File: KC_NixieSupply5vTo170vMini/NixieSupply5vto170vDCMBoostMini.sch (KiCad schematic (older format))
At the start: 40 parts, among them J1 Screw_Terminal_01x04, J2 CONN_01X01, J3 CONN_01X01, J4 CONN_01X01, J5 CONN_01X01, P1 USB_OTG, Q1 FDS2672CT, Q26 MMBTA42, U1 UCC3803

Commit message: Corrected the C6 BOM entry.   Also created a BOM for the MINI version of the layout.
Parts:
- C6: MPN (none) -> C0805C101JAGAC7800
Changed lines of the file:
@@
 F 1 "100pF 250v" H 6700 2200 50  0000 L CNN
 F 2 "Capacitors_SMD:C_0805" H 6738 2250 50  0001 C CNN
-F 3 "" H 6700 2400 50  0000 C CNN
+F 3 "https://www.digikey.com/products/en/capacitors/ceramic-capacitors/60?k=C0805C101JAGAC7800&k=&pkeyword=C0805C101JAGAC7800&pv7=2&quantity=0&ColumnSort=0&page=1&pageSize=25" H 6700 2400 50  0001 C CNN
+F 4 "C0805C101JAGAC7800" H 6700 2400 60  0001 C CNN "MPN"
 	1    6700 2400
 	1    0    0    -1

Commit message: test update
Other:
- moved on the sheet: R7
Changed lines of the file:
@@
 L R R7
 U 1 1 5A408EBF
-P 3050 2650
-F 0 "R7" V 3130 2650 50  0000 C CNN
-F 1 "2k" V 3050 2650 50  0000 C CNN
-F 2 "Resistors_SMD:R_0805" V 2980 2650 50  0001 C CNN
-F 3 "" H 3050 2650 50  0000 C CNN
-	1    3050 2650
+P 2950 2650
+F 0 "R7" V 3030 2650 50  0000 C CNN
+F 1 "2k" V 2950 2650 50  0000 C CNN
+F 2 "Resistors_SMD:R_0805" V 2880 2650 50  0001 C CNN
+F 3 "" H 2950 2650 50  0000 C CNN
+	1    2950 2650
 	-1   0    0    1
 $EndComp
@@
 	4600 4000 4600 3900
 Wire Wire Line
-	4250 2050 5500 2050
-Wire Wire Line
-	5800 2050 6400 2050
+	4250 2050 4600 2050
+Wire Wire Line
+	4600 2050 5250 2050
+Wire Wire Line
+	5250 2050 5500 2050
+Wire Wire Line
+	5800 2050 6150 2050
+Wire Wire Line
+	6150 2050 6250 2050
+Wire Wire Line
+	6250 2050 6400 2050
 Connection ~ 6150 2050
 Wire Wire Line
-	6150 3350 6150 3450
+	6150 3350 6150 3400
+Wire Wire Line
+	6150 3400 6150 3450
 Wire Wire Line
 	6150 3850 6150 3750
@@
 Connection ~ 6150 3400
 Wire Wire Line
-	5250 3400 5600 3400
+	5250 3400 5400 3400
+Wire Wire Line
+	5400 3400 5550 3400
+Wire Wire Line
+	5550 3400 5600 3400
 Wire Wire Line
 	5400 3400 5400 3450
@@
 Connection ~ 5400 3400
 Wire Wire Line
-	6950 2550 6950 2700
-Wire Wire Line
-	6700 2050 7700 2050
-Wire Wire Line
-	8000 2050 8800 2050
+	6950 2550 6950 2650
+Wire Wire Line
+	6950 2650 6950 2700
+Wire Wire Line
+	6700 2050 6800 2050
+Wire Wire Line
+	6800 2050 6950 2050
+Wire Wire Line
+	6950 2050 7150 2050
+Wire Wire Line
+	7150 2050 7350 2050
+Wire Wire Line
+	7350 2050 7550 2050
+Wire Wire Line
+	7550 2050 7700 2050
+Wire Wire Line
+	8000 2050 8150 2050
+Wire Wire Line
+	8150 2050 8650 2050
+Wire Wire Line
+	8650 2050 8800 2050
 Wire Wire Line
 	6950 2050 6950 2250
@@
 	7350 2600 7350 3100
 Wire Wire Line
-	4100 2750 4100 3350
-Wire Wire Line
-	3750 2750 4100 2750
+	4100 2750 4100 3050
+Wire Wire Line
+	4100 3050 4100 3350
+Wire Wire Line
+	3750 2750 3950 2750
+Wire Wire Line
+	3950 2750 4100 2750
 Wire Wire Line
 	3750 2750 3750 2850
 Wire Wire Line
-	3750 3150 3750 3250
+	3750 3150 3750 3200
+Wire Wire Line
+	3750 3200 3750 3250
 Wire Wire Line
 	4100 3500 3950 3500
@@
 	4100 3800 4100 3650
 Wire Wire Line
-	3350 3800 3350 4100
+	3350 3800 3350 3900
+Wire Wire Line
+	3350 3900 3350 4100
 Wire Wire Line
 	3350 4100 3450 4100
@@
 	4250 3900 4250 4100
 Wire Wire Line
-	6700 4100 4150 4100
+	6700 4100 5200 4100
+Wire Wire Line
+	5200 4100 4250 4100
+Wire Wire Line
+	4250 4100 4150 4100
 Connection ~ 4250 4100
 Connection ~ 4600 2050
 Wire Wire Line
-	2200 2050 3950 2050
+	2200 2050 2350 2050
+Wire Wire Line
+	2350 2050 2700 2050
+Wire Wire Line
+	2700 2050 3050 2050
+Wire Wire Line
+	3050 2050 3350 2050
+Wire Wire Line
+	3350 2050 3600 2050
+Wire Wire Line
+	3600 2050 3950 2050
 Wire Wire Line
 	4600 2050 4600 3050
@@
 	6150 3250 6150 3400
 Wire Wire Line
-	5800 2650 6100 2650
+	5800 2650 5900 2650
+Wire Wire Line
+	5900 2650 6000 2650
+Wire Wire Line
+	6000 2650 6100 2650
 Connection ~ 5900 2650
 Connection ~ 6000 2650
@@
 	6100 2400 6150 2400
 Wire Wire Line
-	5900 3250 6150 3250
+	5900 3250 6000 3250
+Wire Wire Line
+	6000 3250 6100 3250
+Wire Wire Line
+	6100 3250 6150 3250
 Connection ~ 6000 3250
 Connection ~ 6100 3250
@@
 Connection ~ 2350 2050
 Wire Wire Line
-	6700 2550 6700 4100
+	6700 2550 6700 2650
+Wire Wire Line
+	6700 2650 6700 4100
 Wire Wire Line
 	7150 2300 7150 2050
@@
 	2350 4500 2350 4400
 Wire Wire Line
-	1850 4200 2050 4200
+	1850 4200 2000 4200
+Wire Wire Line
+	2000 4200 2050 4200
 Wire Wire Line
 	1550 4200 1200 4200
@@
 	3050 3600 3050 3500
 Wire Wire Line
-	3050 2800 3050 3200
-Wire Wire Line
-	3050 2500 3050 2050
+	2950 2800 3050 2950
+Wire Wire Line
+	3050 2950 3050 3050
+Wire Wire Line
+	3050 3050 3050 3200
+Wire Wire Line
+	2950 2500 3050 2050
 Connection ~ 3050 2050
 Connection ~ 3050 3050
@@
 Connection ~ 8650 2050
 Wire Wire Line
-	3350 3800 4100 3800
+	3350 3800 3450 3800
+Wire Wire Line
+	3450 3800 4100 3800
 Wire Wire Line
 	5250 2300 5250 2050
@@
 	3150 2950 3050 2950
 Wire Wire Line
-	2850 3050 3300 3050
+	2850 3050 3050 3050
+Wire Wire Line
+	3050 3050 3300 3050
 Wire Wire Line
 	2850 3050 2850 3800

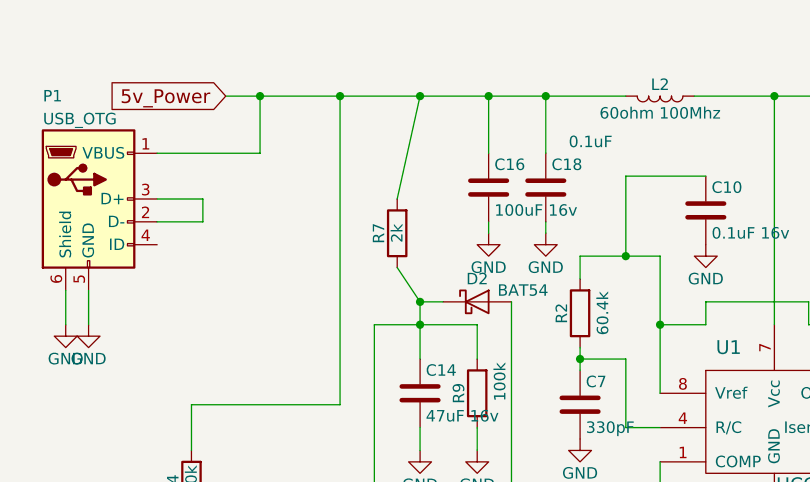
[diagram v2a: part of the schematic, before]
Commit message: Updated the gerber files to include a ground pad for R10 to reduce resistance.  Also updated the net classes for the blog entry.
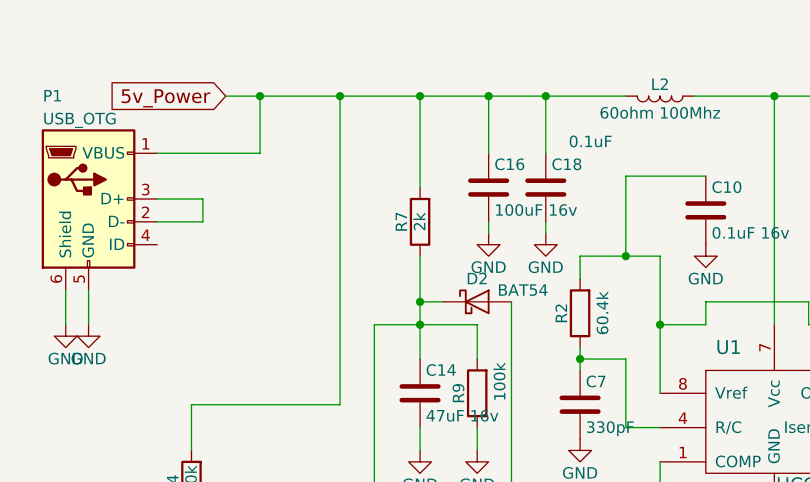
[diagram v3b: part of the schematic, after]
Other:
- moved on the sheet: R7
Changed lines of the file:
@@
 L R R7
 U 1 1 5A408EBF
-P 2950 2650
-F 0 "R7" V 3030 2650 50  0000 C CNN
-F 1 "2k" V 2950 2650 50  0000 C CNN
-F 2 "Resistors_SMD:R_0805" V 2880 2650 50  0001 C CNN
-F 3 "" H 2950 2650 50  0000 C CNN
-	1    2950 2650
+P 3050 2600
+F 0 "R7" V 3130 2600 50  0000 C CNN
+F 1 "2k" V 3050 2600 50  0000 C CNN
+F 2 "Resistors_SMD:R_0805" V 2980 2600 50  0001 C CNN
+F 3 "" H 3050 2600 50  0000 C CNN
+	1    3050 2600
 	-1   0    0    1
 $EndComp
@@
 	3050 3600 3050 3500
 Wire Wire Line
-	2950 2800 3050 2950
+	3050 2750 3050 2950
 Wire Wire Line
 	3050 2950 3050 3050
@@
 	3050 3050 3050 3200
 Wire Wire Line
-	2950 2500 3050 2050
+	3050 2450 3050 2050
 Connection ~ 3050 2050
 Connection ~ 3050 3050
@@
 Connection ~ 3050 2950
 Wire Wire Line
-	3150 2950 3050 2950
+	3050 2950 3150 2950
 Wire Wire Line
 	2850 3050 3050 3050

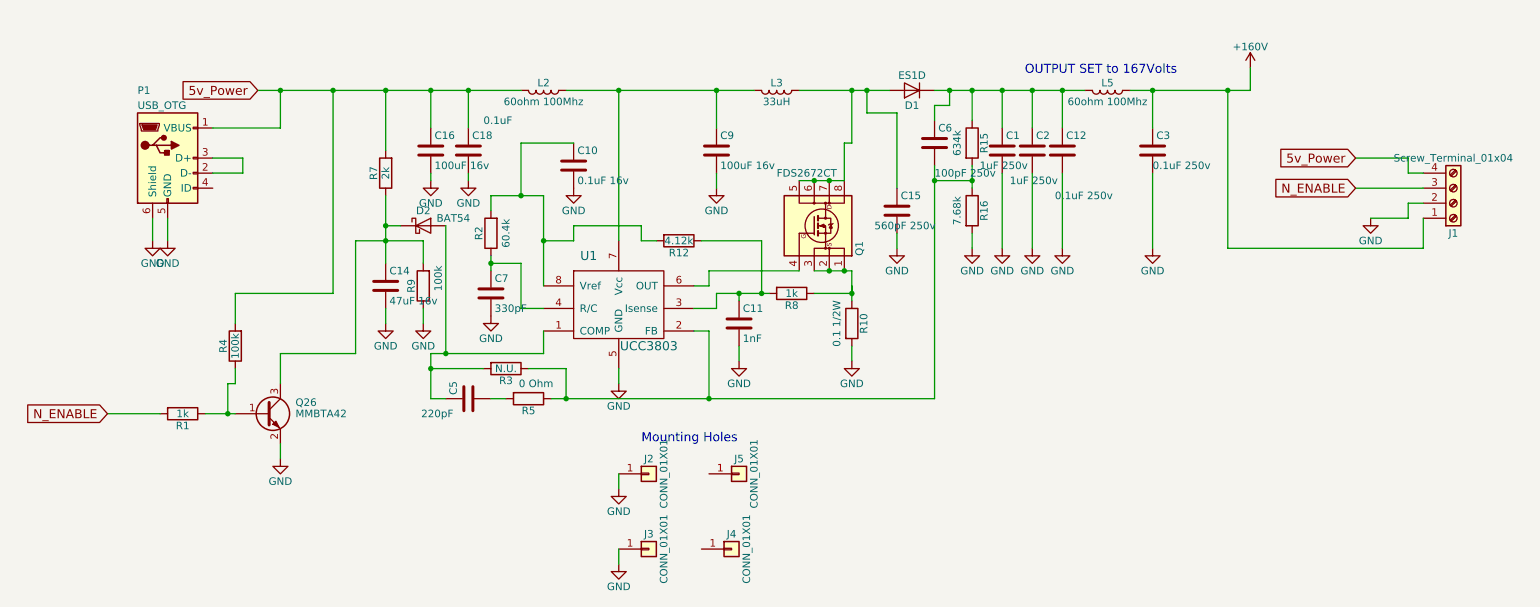
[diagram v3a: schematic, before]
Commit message: New Rev 3 for the Original Nixie Power Supply 1. Corner Mounting Holes are now Solid.  Per the tip by comment reader 2. The original supply has a better ground connection for the USB input,     But the USB connector shield is still grounded. 2.5. The D+ and D- USB inputs are unshorted. 3. The revision was updated to Rev 3 for the Original Supply and Rev 2 for the Mini Supply 4. New Gerbers were created and zip files
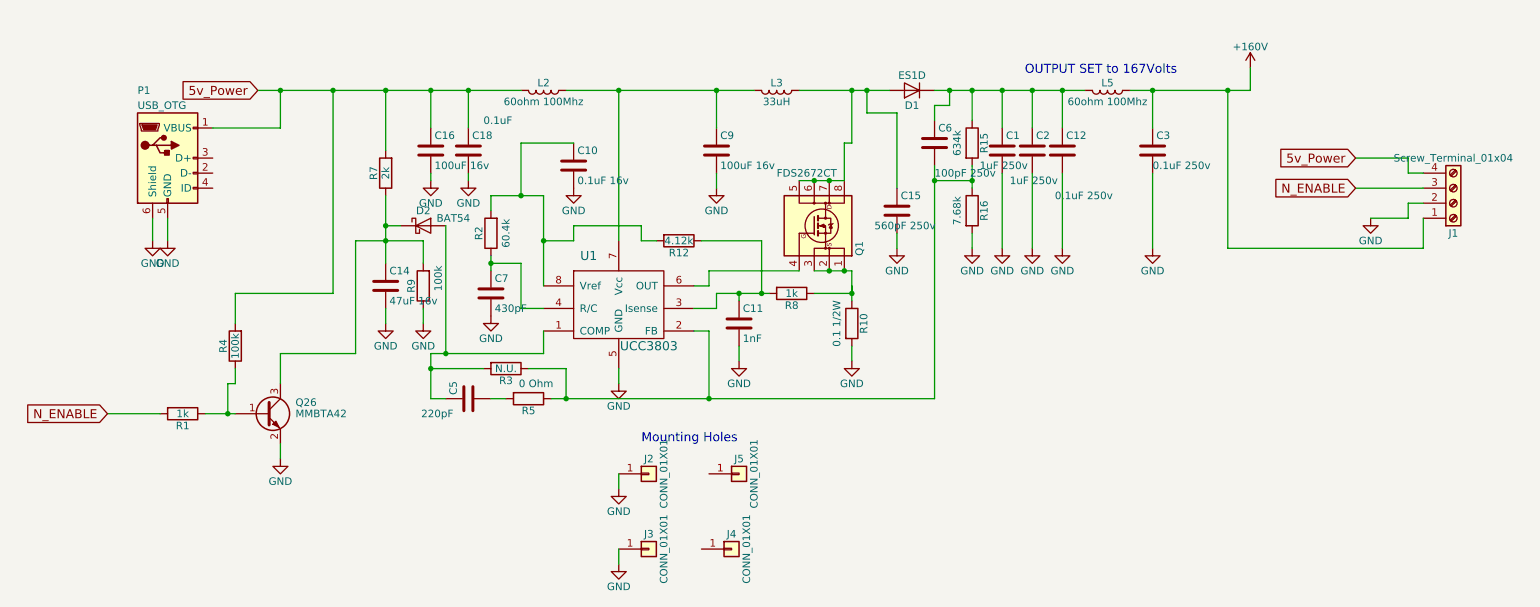
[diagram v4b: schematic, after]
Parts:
- C7: value 330pF -> 430pF; MPN (none) -> CL21C431JBANNNC
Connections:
- net at P1.2 (D-): no longer P1.3 (D+)
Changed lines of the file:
@@
 P 3750 3400
 F 0 "C7" H 3775 3500 50  0000 L CNN
-F 1 "330pF" H 3775 3300 50  0000 L CNN
+F 1 "430pF" H 3775 3300 50  0000 L CNN
 F 2 "Capacitors_SMD:C_0805" H 3788 3250 50  0001 C CNN
-F 3 "" H 3750 3400 50  0000 C CNN
+F 3 "https://www.digikey.com/product-detail/en/samsung-electro-mechanics/CL21C431JBANNNC/1276-2659-1-ND/3890745" H 3750 3400 50  0001 C CNN
+F 4 "CL21C431JBANNNC" H 3750 3400 60  0001 C CNN "MPN"
 	1    3750 3400
 	1    0    0    -1
@@
 F 3 "" H 3750 3550 50  0000 C CNN
 	1    3750 3550
-	1    0    0    -1
-$EndComp
-$Comp
-L GND #PWR09
-U 1 1 5885B65A
-P 1500 3050
-F 0 "#PWR09" H 1500 2800 50  0001 C CNN
-F 1 "GND" H 1500 2900 50  0000 C CNN
-F 2 "" H 1500 3050 50  0000 C CNN
-F 3 "" H 1500 3050 50  0000 C CNN
-	1    1500 3050
 	1    0    0    -1
 $EndComp
@@
 $EndComp
 $Comp
-L GND #PWR010
+L GND #PWR09
 U 1 1 5960F6F8
 P 3350 2650
-F 0 "#PWR010" H 3350 2400 50  0001 C CNN
+F 0 "#PWR09" H 3350 2400 50  0001 C CNN
 F 1 "GND" H 3350 2500 50  0000 C CNN
 F 2 "" H 3350 2650 50  0000 C CNN
@@
 $EndComp
 $Comp
-L GND #PWR011
+L GND #PWR010
 U 1 1 59701877
 P 1600 3050
-F 0 "#PWR011" H 1600 2800 50  0001 C CNN
+F 0 "#PWR010" H 1600 2800 50  0001 C CNN
 F 1 "GND" H 1600 2900 50  0000 C CNN
 F 2 "" H 1600 3050 50  0000 C CNN
@@
 $EndComp
 $Comp
-L GND #PWR012
+L GND #PWR011
 U 1 1 597060B9
 P 7150 3100
-F 0 "#PWR012" H 7150 2850 50  0001 C CNN
+F 0 "#PWR011" H 7150 2850 50  0001 C CNN
 F 1 "GND" H 7150 2950 50  0000 C CNN
 F 2 "" H 7150 3100 50  0000 C CNN
@@
 $EndComp
 $Comp
-L GND #PWR013
+L GND #PWR012
 U 1 1 59706564
 P 7550 3100
-F 0 "#PWR013" H 7550 2850 50  0001 C CNN
+F 0 "#PWR012" H 7550 2850 50  0001 C CNN
 F 1 "GND" H 7550 2950 50  0000 C CNN
 F 2 "" H 7550 3100 50  0000 C CNN
@@
 $EndComp
 $Comp
-L GND #PWR014
+L GND #PWR013
 U 1 1 597066D0
 P 8150 3100
-F 0 "#PWR014" H 8150 2850 50  0001 C CNN
+F 0 "#PWR013" H 8150 2850 50  0001 C CNN
 F 1 "GND" H 8150 2950 50  0000 C CNN
 F 2 "" H 8150 3100 50  0000 C CNN
@@
 $EndComp
 $Comp
-L GND #PWR015
+L GND #PWR014
 U 1 1 5A408C45
 P 3050 3600
-F 0 "#PWR015" H 3050 3350 50  0001 C CNN
+F 0 "#PWR014" H 3050 3350 50  0001 C CNN
 F 1 "GND" H 3050 3450 50  0000 C CNN
 F 2 "" H 3050 3600 50  0000 C CNN
@@
 $EndComp
 $Comp
-L GND #PWR016
+L GND #PWR015
 U 1 1 5A409296
 P 3300 3600
-F 0 "#PWR016" H 3300 3350 50  0001 C CNN
+F 0 "#PWR015" H 3300 3350 50  0001 C CNN
 F 1 "GND" H 3300 3450 50  0000 C CNN
 F 2 "" H 3300 3600 50  0000 C CNN
@@
 $EndComp
 $Comp
-L GND #PWR017
+L GND #PWR016
 U 1 1 5A40B17A
 P 3600 2650
-F 0 "#PWR017" H 3600 2400 50  0001 C CNN
+F 0 "#PWR016" H 3600 2400 50  0001 C CNN
 F 1 "GND" H 3600 2500 50  0000 C CNN
 F 2 "" H 3600 2650 50  0000 C CNN
@@
 $EndComp
 $Comp
-L GND #PWR018
+L GND #PWR017
 U 1 1 5A460588
 P 9600 2900
-F 0 "#PWR018" H 9600 2650 50  0001 C CNN
+F 0 "#PWR017" H 9600 2650 50  0001 C CNN
 F 1 "GND" H 9600 2750 50  0000 C CNN
 F 2 "" H 9600 2900 50  0000 C CNN
@@
 $EndComp
 $Comp
-L GND #PWR019
+L GND #PWR018
 U 1 1 5A46B995
 P 5250 2700
-F 0 "#PWR019" H 5250 2450 50  0001 C CNN
+F 0 "#PWR018" H 5250 2450 50  0001 C CNN
 F 1 "GND" H 5250 2550 50  0000 C CNN
 F 2 "" H 5250 2700 50  0000 C CNN
@@
 $EndComp
 $Comp
-L GND #PWR020
+L GND #PWR019
 U 1 1 5A47271C
 P 4600 5200
-F 0 "#PWR020" H 4600 4950 50  0001 C CNN
+F 0 "#PWR019" H 4600 4950 50  0001 C CNN
 F 1 "GND" H 4600 5050 50  0000 C CNN
 F 2 "" H 4600 5200 50  0000 C CNN
@@
 $EndComp
 $Comp
-L GND #PWR021
+L GND #PWR020
 U 1 1 5A4727AE
 P 4600 4700
-F 0 "#PWR021" H 4600 4450 50  0001 C CNN
+F 0 "#PWR020" H 4600 4450 50  0001 C CNN
 F 1 "GND" H 4600 4550 50  0000 C CNN
 F 2 "" H 4600 4700 50  0000 C CNN
@@
 $EndComp
 $Comp
-L GND #PWR022
+L GND #PWR021
 U 1 1 5A4786FA
 P 4300 2700
-F 0 "#PWR022" H 4300 2450 50  0001 C CNN
+F 0 "#PWR021" H 4300 2450 50  0001 C CNN
 F 1 "GND" H 4300 2550 50  0000 C CNN
 F 2 "" H 4300 2700 50  0000 C CNN
@@
 $EndComp
 $Comp
-L GND #PWR023
+L GND #PWR022
 U 1 1 5A3FB941
 P 2350 4500
-F 0 "#PWR023" H 2350 4250 50  0001 C CNN
+F 0 "#PWR022" H 2350 4250 50  0001 C CNN
 F 1 "GND" H 2350 4350 50  0000 C CNN
 F 2 "" H 2350 4500 50  0000 C CNN
@@
 	4600 4000 4600 3900
 Wire Wire Line
-	4250 2050 4600 2050
-Wire Wire Line
-	4600 2050 5250 2050
-Wire Wire Line
-	5250 2050 5500 2050
-Wire Wire Line
-	5800 2050 6150 2050
-Wire Wire Line
-	6150 2050 6250 2050
-Wire Wire Line
-	6250 2050 6400 2050
+	4250 2050 5500 2050
+Wire Wire Line
+	5800 2050 6400 2050
 Connection ~ 6150 2050
 Wire Wire Line
-	6150 3350 6150 3400
-Wire Wire Line
-	6150 3400 6150 3450
+	6150 3350 6150 3450
 Wire Wire Line
 	6150 3850 6150 3750
@@
 Connection ~ 6150 3400
 Wire Wire Line
-	5250 3400 5400 3400
-Wire Wire Line
-	5400 3400 5550 3400
-Wire Wire Line
-	5550 3400 5600 3400
+	5250 3400 5600 3400
 Wire Wire Line
 	5400 3400 5400 3450
@@
 Connection ~ 5400 3400
 Wire Wire Line
-	6950 2550 6950 2650
-Wire Wire Line
-	6950 2650 6950 2700
-Wire Wire Line
-	6700 2050 6800 2050
-Wire Wire Line
-	6800 2050 6950 2050
-Wire Wire Line
-	6950 2050 7150 2050
-Wire Wire Line
-	7150 2050 7350 2050
-Wire Wire Line
-	7350 2050 7550 2050
-Wire Wire Line
-	7550 2050 7700 2050
-Wire Wire Line
-	8000 2050 8150 2050
-Wire Wire Line
-	8150 2050 8650 2050
-Wire Wire Line
-	8650 2050 8800 2050
+	6950 2550 6950 2700
+Wire Wire Line
+	6700 2050 7700 2050
+Wire Wire Line
+	8000 2050 8800 2050
 Wire Wire Line
 	6950 2050 6950 2250
@@
 	7350 2600 7350 3100
 Wire Wire Line
-	4100 2750 4100 3050
-Wire Wire Line
-	4100 3050 4100 3350
-Wire Wire Line
-	3750 2750 3950 2750
-Wire Wire Line
-	3950 2750 4100 2750
+	4100 2750 4100 3350
+Wire Wire Line
+	3750 2750 4100 2750
 Wire Wire Line
 	3750 2750 3750 2850
 Wire Wire Line
-	3750 3150 3750 3200
-Wire Wire Line
-	3750 3200 3750 3250
+	3750 3150 3750 3250
 Wire Wire Line
 	4100 3500 3950 3500
@@
 	4100 3800 4100 3650
 Wire Wire Line
-	3350 3800 3350 3900
-Wire Wire Line
-	3350 3900 3350 4100
+	3350 3800 3350 4100
 Wire Wire Line
 	3350 4100 3450 4100
@@
 	4250 3900 4250 4100
 Wire Wire Line
-	6700 4100 5200 4100
-Wire Wire Line
-	5200 4100 4250 4100
-Wire Wire Line
-	4250 4100 4150 4100
+	6700 4100 4150 4100
 Connection ~ 4250 4100
 Connection ~ 4600 2050
 Wire Wire Line
-	2200 2050 2350 2050
-Wire Wire Line
-	2350 2050 2700 2050
-Wire Wire Line
-	2700 2050 3050 2050
-Wire Wire Line
-	3050 2050 3350 2050
-Wire Wire Line
-	3350 2050 3600 2050
-Wire Wire Line
-	3600 2050 3950 2050
+	2200 2050 3950 2050
 Wire Wire Line
 	4600 2050 4600 3050
@@
 	6150 3250 6150 3400
 Wire Wire Line
-	5800 2650 5900 2650
-Wire Wire Line
-	5900 2650 6000 2650
-Wire Wire Line
-	6000 2650 6100 2650
+	5800 2650 6100 2650
 Connection ~ 5900 2650
 Connection ~ 6000 2650
@@
 	6100 2400 6150 2400
 Wire Wire Line
-	5900 3250 6000 3250
-Wire Wire Line
-	6000 3250 6100 3250
-Wire Wire Line
-	6100 3250 6150 3250
+	5900 3250 6150 3250
 Connection ~ 6000 3250
 Connection ~ 6100 3250
@@
 Connection ~ 2350 2050
 Wire Wire Line
-	6700 2550 6700 2650
-Wire Wire Line
-	6700 2650 6700 4100
+	6700 2550 6700 4100
 Wire Wire Line
 	7150 2300 7150 2050
@@
 Wire Wire Line
 	1600 3050 1600 2900
-Wire Wire Line
-	1500 2900 1500 3050
 Wire Wire Line
 	5200 3650 5200 4100
@@
 	2350 4500 2350 4400
 Wire Wire Line
-	1850 4200 2000 4200
-Wire Wire Line
-	2000 4200 2050 4200
+	1850 4200 2050 4200
 Wire Wire Line
 	1550 4200 1200 4200
@@
 	3050 3600 3050 3500
 Wire Wire Line
-	3050 2750 3050 2950
-Wire Wire Line
-	3050 2950 3050 3050
-Wire Wire Line
-	3050 3050 3050 3200
+	3050 2750 3050 3200
 Wire Wire Line
 	3050 2450 3050 2050
@@
 Connection ~ 8650 2050
 Wire Wire Line
-	3350 3800 3450 3800
-Wire Wire Line
-	3450 3800 4100 3800
+	3350 3800 4100 3800
 Wire Wire Line
 	5250 2300 5250 2050
@@
 	4300 3050 4100 3050
 Wire Wire Line
-	1900 2500 2100 2500
-Wire Wire Line
-	2100 2500 2100 2600
-Wire Wire Line
-	2100 2600 1900 2600
-Wire Wire Line
 	9850 2500 9850 2600
 Wire Wire Line
@@
 	3050 2950 3150 2950
 Wire Wire Line
-	2850 3050 3050 3050
-Wire Wire Line
-	3050 3050 3300 3050
+	2850 3050 3300 3050
 Wire Wire Line
 	2850 3050 2850 3800
@@
 	1    0    0    -1
 $EndComp
+$Comp
+L GND #PWR023
+U 1 1 5885B65A
+P 1500 3050
+F 0 "#PWR023" H 1500 2800 50  0001 C CNN
+F 1 "GND" H 1500 2900 50  0000 C CNN
+F 2 "" H 1500 3050 50  0000 C CNN
+F 3 "" H 1500 3050 50  0000 C CNN
+	1    1500 3050
+	1    0    0    -1
+$EndComp
+Wire Wire Line
+	1500 2900 1500 3050
 $EndSCHEMATC
